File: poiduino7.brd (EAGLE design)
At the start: 160 x 100 mm, 17 parts, among them Y1 16MHZ

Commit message: add gitignore and new board
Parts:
- added C6, C7: 0.1uf, Seeed-Capacitor:CERAMIC-2.54
- added K1: TS-1109, Seeed-OPL-Button:SW4-6.0X6.0X5.0MM
- C1, C2: value 10nf -> 18pf
- C3, C4: value 10nf -> 0.1uf
- C5: value 100uf -> 1uf
- moved JP1 111.1 mm to (66.0, 17.8), turned to 270 degrees
- moved JP5 104.1 mm to (57.1, 2.54)
- moved C1 100.1 mm to (50.5, 46.0), turned to 225 degrees
- moved JP4 79.8 mm to (54.6, 50.8), turned to 180 degrees
- moved Y1 79.3 mm to (48.4, 37.9), turned to 135 degrees
- moved JP2 74.0 mm to (39.4, 2.54)
- moved C2 68.7 mm to (51.6, 42.1)
- moved JP3 60.2 mm to (33.0, 50.8)
- moved D2 58.0 mm to (7.62, 39.4)
- moved R1 56.6 mm to (34.3, 7.62)
- moved D1 53.9 mm to (15.7, 18.5), turned to 180 degrees
- moved R3 50.9 mm to (6.35, 30.5), turned to 90 degrees
- moved R2 46.0 mm to (14.2, 27.2), turned to 45 degrees
- moved C4 42.1 mm to (12.4, 44.5), turned to 135 degrees
- moved C3 28.4 mm to (5.08, 45.7), turned to 225 degrees
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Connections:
- removed net N$10: U1.22
- removed net N$11: U1.7
- removed net N$12: U1.8
- removed net N$13: U1.19
- removed net N$14: U1.18
- removed net N$15: U1.17
- removed net N$16: U1.16
- removed net N$17: U1.15
- removed net N$18: U1.14
- removed net N$19: U1.27
- removed net N$2: C2.2, Y1.1
- removed net N$20: U1.26
- removed net N$21: U1.25
- removed net N$22: U1.24
- removed net N$23: U1.23
- removed net N$24: U1.13
- removed net N$25: U1.12
- removed net N$26: U1.11
- removed net N$27: U1.6
- removed net N$28: U1.5
- removed net N$29: U1.4
- removed net N$30: U1.3
- removed net N$31: U1.2
- removed net N$4: U1.28
- removed net N$5: U1.9
- removed net N$7: U1.1
- removed net N$8: U1.21
- removed net N$9: U1.20
- new net A0: JP5.1, U1.23
- new net A1: JP5.2, U1.24
- new net A2: JP5.3, U1.25
- new net A3: JP5.4, U1.26
- new net A4-SDA: JP5.5, U1.27
- new net A5-SCL: JP5.6, U1.28
- new net AREF: C4.2, JP3.1, U1.21
- new net AVCC: C7.2, U1.20
- new net CTS: JP1.5
- new net DTR: C6.2, JP1.1
- new net N$34: JP2.1
- new net N$38: JP2.5
- new net PIN10: JP3.6, U1.16
- new net PIN11: JP3.5, U1.17
- new net PIN12: JP3.4, U1.18
- new net PIN13: JP3.3, R2.2, U1.19
- new net PIN2: JP4.3, U1.4
- new net PIN3: JP4.4, U1.5
- new net PIN4: JP4.5, U1.6
- new net PIN5: JP4.6, U1.11
- new net PIN6: JP4.7, U1.12
- new net PIN7: JP4.8, U1.13
- new net PIN8: JP3.8, U1.14
- new net PIN9: JP3.7, U1.15
- new net RESET: C6.1, JP2.6, K1.1, K1.4, R1.2, U1.1
- new net RXD: JP1.2, JP4.1, U1.2
- new net TXD: JP1.3, JP4.2, U1.3
- new net VCC: C3.2, C5.+, C7.1, JP1.4, JP2.4, R1.1, R3.1, U1.7
- new net XTAL1: C2.2, U1.9, Y1.1
- new net XTAL2: C1.2, U1.10, Y1.2
- net GND: now also C3.1, C4.1, C5.-, D1.K, D2.K, JP1.6, JP2.2, JP2.3, JP3.2, K1.2, U1.22, U1.8
- net N$3: now also D2.A, R3.2; no longer C1.2, Y1.2
- net N$6: now also D1.A, R2.1; no longer U1.10
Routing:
- net GND: track 0.00 -> 256.4 mm
- net VCC: track 0.00 -> 176.4 mm, vias 0 -> 2
- net AREF: track 0.00 -> 63.8 mm
- net RESET: track 0.00 -> 62.1 mm, vias 0 -> 2
- net RXD: track 0.00 -> 61.1 mm
- net TXD: track 0.00 -> 47.5 mm
- net PIN13: track 0.00 -> 46.1 mm
- net PIN12: track 0.00 -> 33.7 mm
- net PIN2: track 0.00 -> 29.2 mm
- net PIN11: track 0.00 -> 29.0 mm
- net PIN3: track 0.00 -> 27.9 mm
- net PIN4: track 0.00 -> 26.4 mm
- net PIN10: track 0.00 -> 23.8 mm
- net A0: track 0.00 -> 22.2 mm
- net A1: track 0.00 -> 20.7 mm
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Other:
- board size 160 x 100 mm -> 67.8 x 53.4 mm

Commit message: new board
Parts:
- C7: device Seeed-Capacitor:CERAMIC-2.54 -> capacitor-wima:C5B2.5
- moved C5 10.3 mm to (12.5, 27.1), turned to 270 degrees
- moved C3 7.73 mm to (3.86, 38.1), turned to 270.6 degrees
- moved D1 7.69 mm to (23.3, 19.8), turned to 270 degrees
- moved JP1 7.28 mm to (59.0, 19.7)
- moved JP3 7.28 mm to (26.0, 52.8)
- moved C1 7.28 mm to (43.5, 47.9)
- moved JP4 7.28 mm to (47.6, 52.8)
- moved JP2 7.28 mm to (32.4, 4.49)
- moved JP5 7.28 mm to (50.1, 4.49)
- moved C2 7.28 mm to (44.6, 44.0)
- moved K1 7.28 mm to (60.9, 38.7)
- moved U1 7.28 mm to (38.7, 29.9)
- moved Y1 7.28 mm to (41.4, 39.9)
- moved C6 7.28 mm to (59.0, 30.5)
- moved R1 6.16 mm to (28.5, 9.61)
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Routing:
- net VCC: track 176.4 -> 153.8 mm, vias 2 -> 0
- net AREF: track 63.8 -> 47.8 mm
- net GND: track 256.4 -> 241.4 mm, vias 0 -> 2
- net PIN13: track 46.1 -> 38.6 mm
- net AVCC: track 13.3 -> 6.32 mm
- net XTAL1: track 12.7 -> 14.3 mm
- net RESET: track 62.1 -> 60.9 mm
- added copper zone on layer 16, net GND
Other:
- board size 67.8 x 53.4 mm -> 69.6 x 56.9 mm

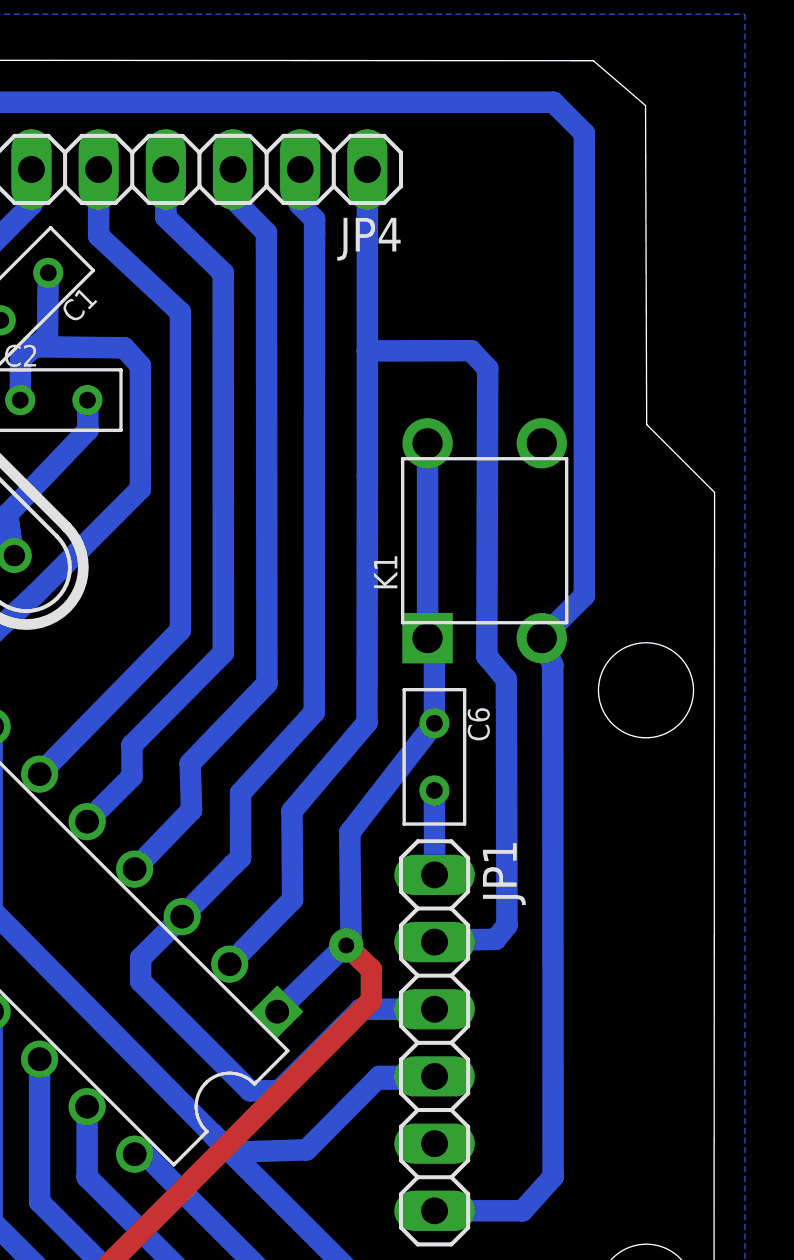
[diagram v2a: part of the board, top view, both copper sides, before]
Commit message: rename file and folders, generate gcode and simulate files for Roland
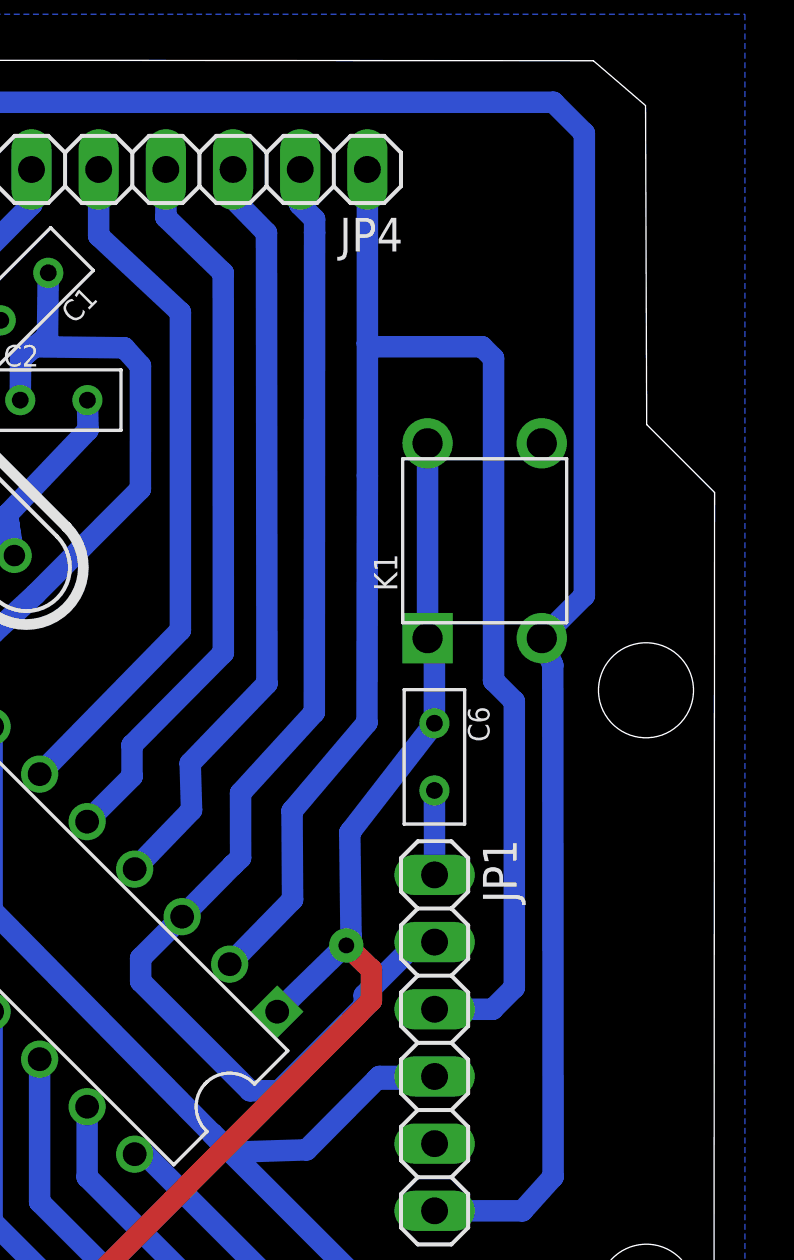
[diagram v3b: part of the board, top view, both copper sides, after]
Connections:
- net RXD: now also JP1.3; no longer JP1.2
- net TXD: now also JP1.2; no longer JP1.3
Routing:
- net RXD: track 61.2 -> 64.5 mm
- net TXD: track 47.7 -> 49.0 mm
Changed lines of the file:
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@@
 <?xml version="1.0" encoding="utf-8"?>
 <!DOCTYPE eagle SYSTEM "eagle.dtd">
-<eagle version="9.0.0">
+<eagle version="8.6.0">
 <drawing>
 <settings>
@@
 <grid distance="0.000123031496" unitdist="mil" unit="mil" style="lines" multiple="1" display="no" altdistance="0.000123031496" altunitdist="mil" altunit="mil"/>
 <layers>
-<layer number="1" name="Top" color="4" fill="1" visible="yes" active="yes"/>
+<layer number="1" name="Top" color="4" fill="1" visible="no" active="yes"/>
 <layer number="2" name="Route2" color="1" fill="3" visible="no" active="no"/>
 <layer number="3" name="Route3" color="4" fill="3" visible="no" active="no"/>
@@
 <layer number="17" name="Pads" color="2" fill="1" visible="yes" active="yes"/>
 <layer number="18" name="Vias" color="2" fill="1" visible="yes" active="yes"/>
-<layer number="19" name="Unrouted" color="6" fill="1" visible="no" active="yes"/>
+<layer number="19" name="Unrouted" color="6" fill="1" visible="yes" active="yes"/>
 <layer number="20" name="Dimension" color="24" fill="1" visible="yes" active="yes"/>
 <layer number="21" name="tPlace" color="7" fill="1" visible="yes" active="yes"/>
@@
 </signal>
 <signal name="RXD">
-<contactref element="JP1" pad="2"/>
 <contactref element="U1" pad="2"/>
 <contactref element="JP4" pad="1"/>
@@
 <wire x1="53.64088125" y1="28.495028125" x2="56.47448125" y2="31.8385875" width="0.8128" layer="16"/>
 <wire x1="56.47448125" y1="31.8385875" x2="56.490628125" y2="41.17596875" width="0.8128" layer="16"/>
-<wire x1="56.490628125" y1="41.17596875" x2="56.490628125" y2="45.89325625" width="0.8128" layer="16"/>
-<wire x1="56.490628125" y1="45.89325625" x2="56.490628125" y2="52.752484375" width="0.8128" layer="16"/>
-<wire x1="59.030628125" y1="23.542484375" x2="59.10301875" y2="23.614875" width="0.8128" layer="16"/>
-<wire x1="59.10301875" y1="23.614875" x2="61.3340875" y2="23.64456875" width="0.8128" layer="16"/>
-<wire x1="61.3340875" y1="23.64456875" x2="61.767178125" y2="24.174321875" width="0.8128" layer="16"/>
-<wire x1="61.767178125" y1="24.174321875" x2="61.747378125" y2="33.4659" width="0.8128" layer="16"/>
-<wire x1="61.747378125" y1="33.4659" x2="61.0051875" y2="34.34880625" width="0.8128" layer="16"/>
-<wire x1="61.0051875" y1="34.34880625" x2="61.039115625" y2="45.22158125" width="0.8128" layer="16"/>
-<wire x1="61.039115625" y1="45.22158125" x2="60.408696875" y2="45.900415625" width="0.8128" layer="16"/>
-<wire x1="60.408696875" y1="45.900415625" x2="56.490628125" y2="45.89325625" width="0.8128" layer="16"/>
+<wire x1="56.490628125" y1="41.17596875" x2="56.490628125" y2="46.172559375" width="0.8128" layer="16"/>
+<contactref element="JP1" pad="3"/>
+<wire x1="56.490628125" y1="46.172559375" x2="56.490628125" y2="52.752484375" width="0.8128" layer="16"/>
+<wire x1="59.030628125" y1="21.002484375" x2="61.226303125" y2="21.002484375" width="0.8128" layer="16"/>
+<wire x1="62.045" y1="32.64408125" x2="61.259225" y2="33.42985625" width="0.8128" layer="16"/>
+<wire x1="61.259225" y1="33.42985625" x2="61.259225" y2="45.615440625" width="0.8128" layer="16"/>
+<wire x1="61.259225" y1="45.615440625" x2="60.825315625" y2="46.04935" width="0.8128" layer="16"/>
+<wire x1="60.825315625" y1="46.04935" x2="56.6138375" y2="46.04935" width="0.8128" layer="16"/>
+<wire x1="56.6138375" y1="46.04935" x2="56.490628125" y2="46.172559375" width="0.8128" layer="16"/>
+<wire x1="61.226303125" y1="21.002484375" x2="62.045" y2="21.82118125" width="0.8128" layer="16"/>
+<wire x1="62.045" y1="21.82118125" x2="62.045" y2="32.64408125" width="0.8128" layer="16"/>
 </signal>
 <signal name="TXD">
-<contactref element="JP1" pad="3"/>
 <contactref element="U1" pad="3"/>
 <contactref element="JP4" pad="2"/>
@@
 <wire x1="47.917546875" y1="22.05668125" x2="52.0522" y2="17.922028125" width="0.8128" layer="16"/>
 <wire x1="52.0522" y1="17.922028125" x2="53.1563875" y2="17.922028125" width="0.8128" layer="16"/>
-<wire x1="53.1563875" y1="17.922028125" x2="56.23684375" y2="21.002484375" width="0.8128" layer="16"/>
-<wire x1="56.23684375" y1="21.002484375" x2="59.030628125" y2="21.002484375" width="0.8128" layer="16"/>
 <wire x1="53.950628125" y1="52.752484375" x2="53.9359125" y2="51.42780625" width="0.8128" layer="16"/>
 <wire x1="53.9359125" y1="51.42780625" x2="54.494378125" y2="50.869340625" width="0.8128" layer="16"/>
@@
 <wire x1="51.696975" y1="26.728465625" x2="51.410659375" y2="26.45666875" width="0.8128" layer="16"/>
 <wire x1="51.410659375" y1="26.45666875" x2="49.486934375" y2="24.504328125" width="0.8128" layer="16"/>
+<contactref element="JP1" pad="2"/>
+<wire x1="56.37054375" y1="21.136184375" x2="56.37054375" y2="21.5357125" width="0.8128" layer="16"/>
+<wire x1="56.37054375" y1="21.5357125" x2="58.377315625" y2="23.542484375" width="0.8128" layer="16"/>
+<wire x1="58.377315625" y1="23.542484375" x2="59.030628125" y2="23.542484375" width="0.8128" layer="16"/>
+<wire x1="53.1563875" y1="17.922028125" x2="56.37054375" y2="21.136184375" width="0.8128" layer="16"/>
 </signal>
 <signal name="CTS">
